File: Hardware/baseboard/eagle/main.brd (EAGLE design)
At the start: 119.5 x 96 mm, 169 parts, among them X1 JST-4POS-2X4POS, X1.2 TACH/LAP, X2 ATLAS-LTC, X2.1 MOTOR, X2.2 VRAILS+, X2.3 5V+SoC, X3 SYS-IIC, X4 SYSTEWI

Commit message: baseboard wip +did layout for 5V DCDC, was really fun to do, TI know their sh…tuff +now integrating into baseboard
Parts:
- added D1: BAS40-05, diode:SOT23
- moved A9:R2 420.6 mm to (79.5, 70.5), turned to 90 degrees
- moved A9:C5 416.9 mm to (77.9, 70.3), turned to 270 degrees
- moved A9:C4 24.6 mm to (89.9, 70.0)
- moved A9:C1 22.9 mm to (74.6, 71.8), turned to 270 degrees
- moved A9:C3 22.0 mm to (87.8, 70.0)
- moved A9:C2 19.5 mm to (85.7, 70.0)
- moved A9:U1 16.9 mm to (82.5, 69.8), turned to 270 degrees
- moved A9:R1 6.94 mm to (82.7, 67.0)
- moved A9:L1 0.56 mm to (79.7, 76.4)
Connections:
- net A9:N$1 renamed A9:CC
- removed net TOP.V+/IPC: A5:R8.2, A5:T2.5, A5:T2.6, A5:T2.7, A5:T2.8, A5:U1.17, S1.2
- new net +4.1V: A5:R8.2, A5:T2.5, A5:T2.6, A5:T2.7, A5:T2.8, A5:U1.17, D1.2, S1.2
- new net N$1: D1.3, X4.1
- net VDD: now also D1.1; no longer X4.1
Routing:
- net +4.1V: track 0.00 -> 42.2 mm, vias 0 -> 2
- net +5V: track 0.00 -> 11.4 mm
- net GND: track 10.0 -> 18.3 mm, vias 6 -> 32
- net A9:✳SW: track 0.00 -> 6.52 mm
- net TOP.V+/IPC: track 4.19 -> 0.00 mm
- net A9:CC: track 0.00 -> 4.09 mm
- net N$1: track 0.00 -> 2.50 mm
- net TOP.INACT: track 0.00 -> 2.17 mm
- added copper zone on layer 1, net +5V
- added copper zone on layer 1, net A9:CC
- added copper zone on layer 1, net A9:✳SW
- added copper zone on layer 1, net VDD
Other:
- board text added: "-> TI's got it down, look up their ref design: think altpart compatible landing pattern"
- board text added: ">thermal via tree algorithm?"
- board text added: "TODO ADD OPT. FB NETWORK BECAUSE LAYOUT"
- board text added: "TODO for final phase: Add stopmask extension for all inductors"
- board text added: "to minimize via/area cost?"
- board text removed: "embedded"
- board text removed: "interface"
- board text removed: "system"
- board text removed: "this was a typo initially"
- board text removed: "two-wire"
- board text removed: "wake-able IRQ"

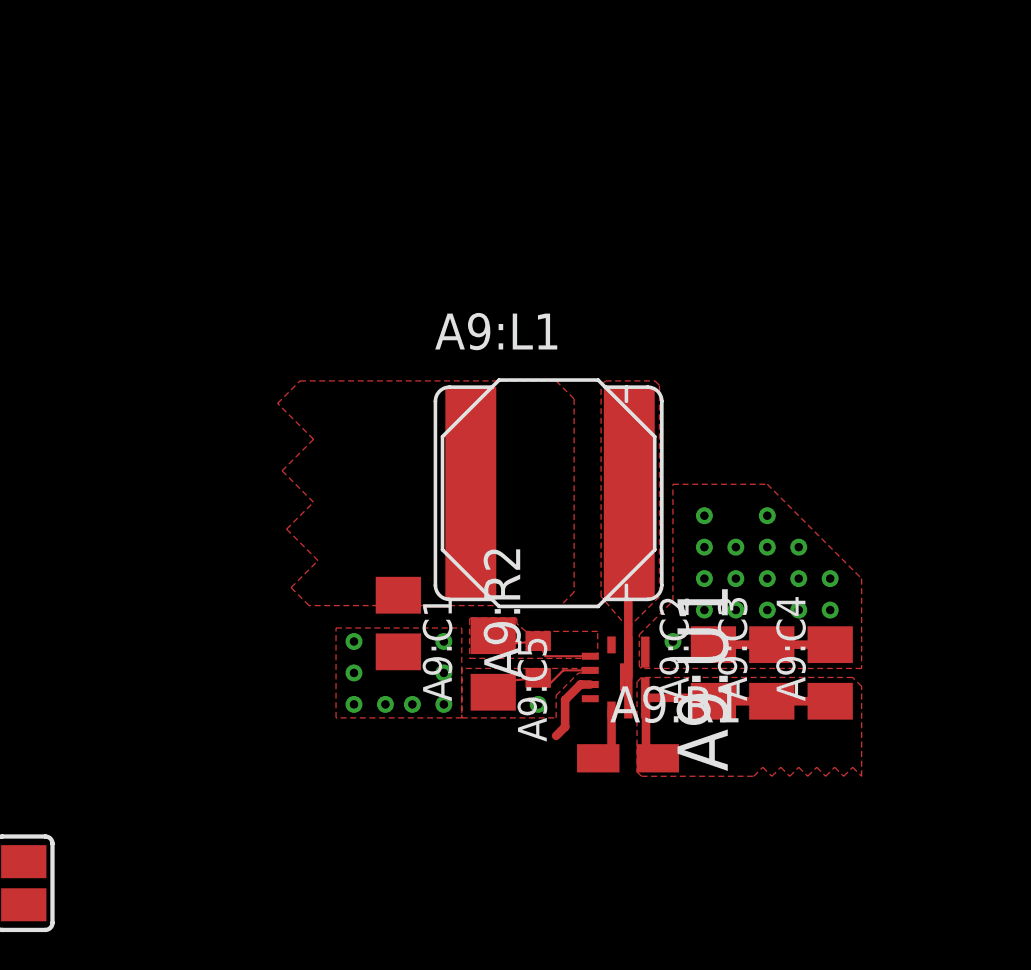
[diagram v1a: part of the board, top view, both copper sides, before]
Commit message: wip of baseboard + had to flip inductor on 5vdcdc because screw post is in the way + more chance it'll fit now
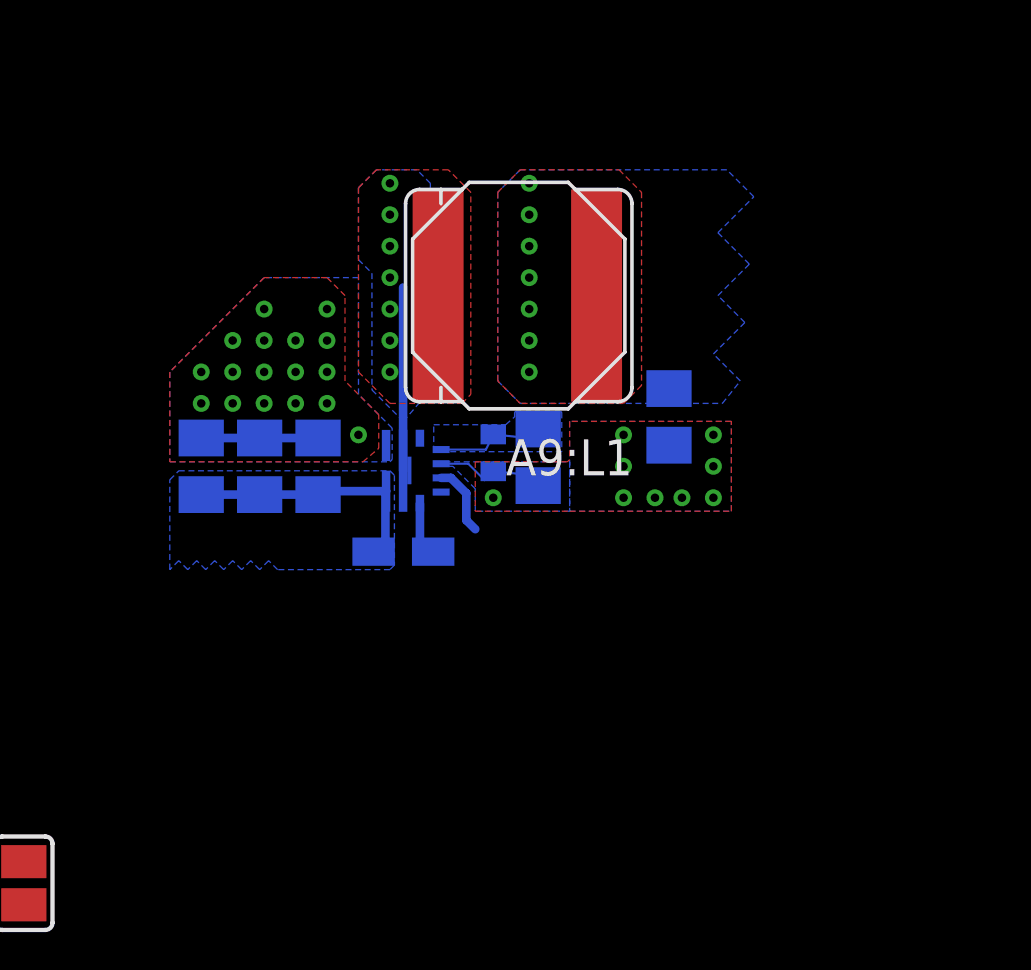
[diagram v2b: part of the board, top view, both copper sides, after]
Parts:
- moved A9:C4 23.4 mm to (67.6, 77.3), flipped to the bottom
- moved A9:C3 19.5 mm to (69.7, 77.3), flipped to the bottom
- moved A9:C2 15.8 mm to (71.8, 77.3), flipped to the bottom
- moved A9:C1 12.0 mm to (84.2, 79.1), flipped to the bottom
- moved A9:R1 10.8 mm to (74.8, 74.3), flipped to the bottom
- moved A9:U1 10.6 mm to (74.9, 77.2), flipped to the bottom
- moved A9:C5 7.47 mm to (79.5, 77.6), flipped to the bottom
- moved A9:R2 7.47 mm to (77.9, 77.8), flipped to the bottom
- moved A9:L1 7.01 mm to (79.1, 83.3), turned to 180 degrees
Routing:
- net A9:✳SW: track 6.52 -> 6.48 mm, vias 0 -> 7
- net VDD: vias 2 -> 9
- added copper zone on layer 16, net +5V
- added copper zone on layer 16, net A9:CC
- added copper zone on layer 16, net A9:✳SW
- added copper zone on layer 16, net VDD
- removed copper zone on layer 1, net +5V
- removed copper zone on layer 1, net A9:CC
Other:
- board text added: "going to flip my shit (ノ°Д°）ノ︵ ┻━┻"
- board text removed: ">thermal via tree algorithm?"
- board text removed: "to minimize via/area cost?"

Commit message: wip baseboard/quicksave + touchdown of dcdc   (quicksave means restore point)
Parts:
- moved A9:C1 89.0 mm to (18.8, 18.6), turned to 90 degrees
- moved A9:L1 88.4 mm to (23.9, 14.3), turned to 0 degrees
- moved A9:C5 80.4 mm to (23.4, 20.0), turned to 90 degrees
- moved A9:R2 78.5 mm to (25.0, 19.9), turned to 270 degrees
- moved A9:U1 73.5 mm to (28.0, 20.5), turned to 90 degrees
- moved A9:C2 69.9 mm to (31.2, 20.3), turned to 270 degrees
- moved A9:R1 69.4 mm to (28.2, 22.8), turned to 180 degrees
- moved A9:C3 67.6 mm to (33.3, 20.3), turned to 270 degrees
- moved A9:C4 65.5 mm to (35.3, 20.3), turned to 270 degrees
- moved REF1 1.12 mm to (-0.06, 0.08)
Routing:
- net TOP.INACT: track 2.17 -> 1.67 mm
- net GND: vias 32 -> 33
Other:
- outline, holes or cut-outs redrawn
- board text added: "+5V"
- board text added: "182 airwires? i don't give a rats' nest."
- board text added: "SMALLER PACKAGE NOW!"
- board text added: "conf"

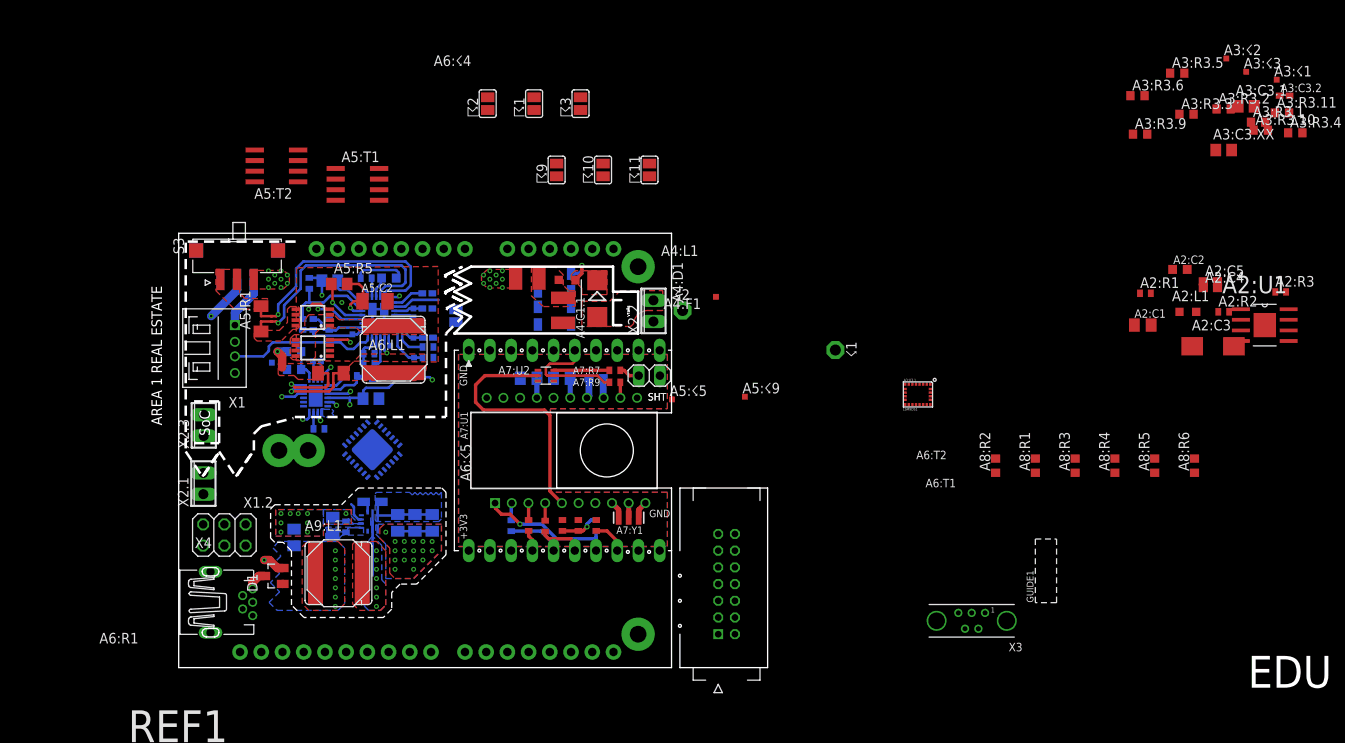
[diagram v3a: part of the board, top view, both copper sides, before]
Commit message: wip baseboard + as announced, added breakaway LTC connector + threw in molex/wirepad power thing too   because it looks symmetrical and the fab house would like   the board to be rectangular I guess
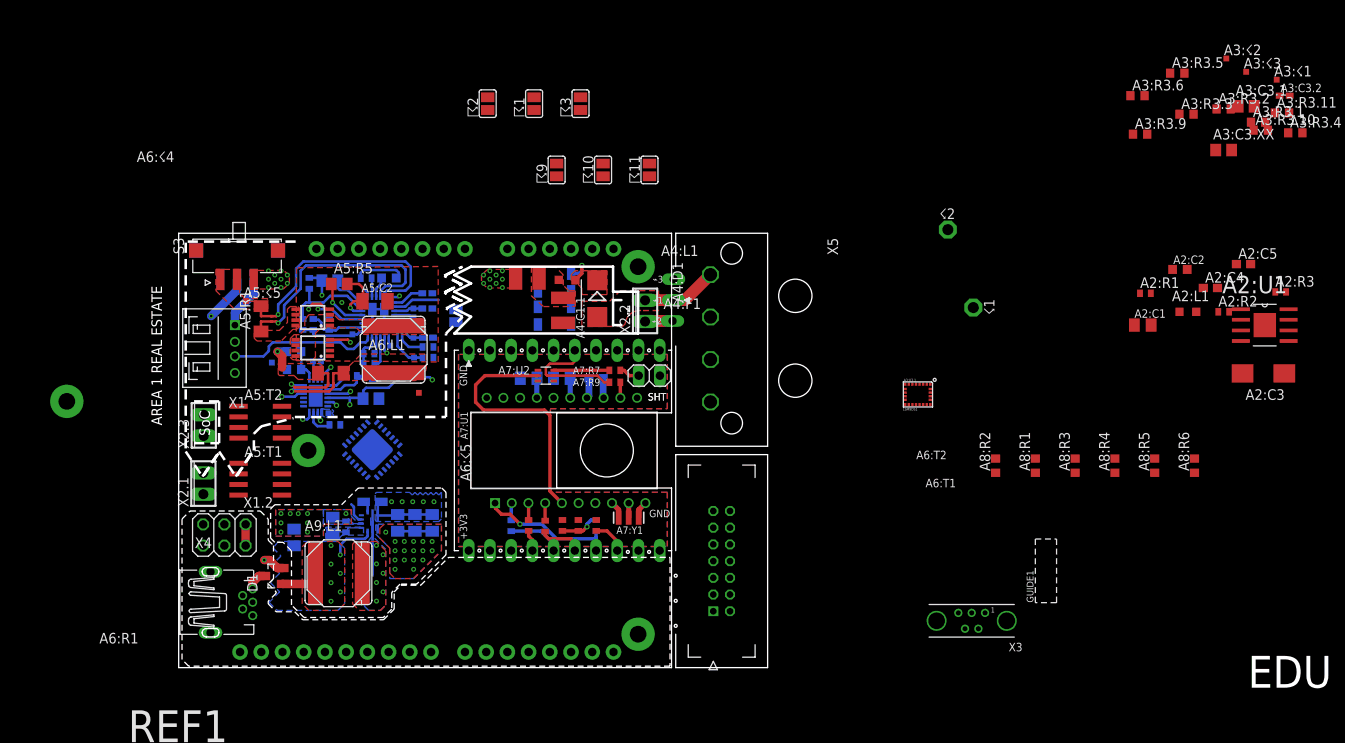
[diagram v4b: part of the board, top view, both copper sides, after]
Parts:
- added X5: 15244441, kitt.con:MOLEX_15244441
- added ⌁1: SINGLEPAD40MIL-BREAK.PILOT, kitt.con:PAD40MIL.BREAK_PILOT
- added ⌁2, ⌁3: SINGLEPAD40MIL-BREAK, kitt.con:PAD40MIL.BREAK
- moved A5:☇5 52.3 mm to (13.1, 46.9)
- moved A5:☇9 49.9 mm to (22.9, 33.4), flipped to the bottom
- moved A6:☇4 37.4 mm to (33.8, 35.9)
- moved A5:T1 37.2 mm to (14.8, 25.6)
- moved ☇2 33.2 mm to (97.1, 55.4)
- moved A5:T2 30.7 mm to (14.8, 32.4), turned to 270 degrees
- moved ☇1 17.3 mm to (100.1, 46.1)
- moved A2:C3 6.85 mm to (134.9, 38.2), turned to 180 degrees
- moved A2:C5 4.47 mm to (132.5, 51.3)
- moved X2 2.81 mm to (70.0, 15.8)
- moved A6:C1 1.96 mm to (23.7, 32.1)
- moved X2.2 1.00 mm to (60.8, 45.7)
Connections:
- net +5V: now also X5.4, ⌁3.P$1
- net GND: now also X5.2, X5.3, ⌁2.P$1
- net VCC/2: now also X5.1, ⌁1.P$1
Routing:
- net VCC/2: track 0.00 -> 9.10 mm
- net VDD: track 15.3 -> 23.9 mm
- net GND: track 18.3 -> 26.3 mm
- net +3V3: track 11.3 -> 13.9 mm
- net VF+OUT/SWITCH: track 0.00 -> 2.03 mm
- net +5V: track 11.2 -> 13.0 mm
- net A6:TRACK/SS: track 2.00 -> 3.38 mm
- added copper zone on layer 15, net +5V
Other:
- outline, holes or cut-outs redrawn
- board text added: "A BUNCH OF WIRES"
- board text added: "AREA 4: LOGIC"
- board text added: "…this isn't working. ~ Gabe N."
- board text removed: "SMALLER PACKAGE NOW!"

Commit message: wip baseboard quicksave  + now working on motor driver  + board area left is really, really tiny  + totally doable tough
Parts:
- removed X3: SYS-IIC, kitt.con:651005136421
- moved A5:T2 57.8 mm to (23.7, 89.5)
- moved A5:T1 56.6 mm to (23.7, 81.4)
- moved A2:C5 20.5 mm to (115.4, 40.0), flipped to the bottom, turned to 270 degrees
- moved A2:C3 17.6 mm to (119.2, 46.2), flipped to the bottom
- moved A2:U1 15.1 mm to (120.1, 41.4), turned to 180 degrees
- moved A2:R3 14.8 mm to (124.1, 40.7), flipped to the bottom, turned to 270 degrees
- moved A2:C4 14.1 mm to (115.4, 43.3), flipped to the bottom, turned to 270 degrees
- moved A2:C2 11.8 mm to (113.1, 50.2), flipped to the bottom
- moved A2:C1 10.8 mm to (113.0, 51.9), flipped to the bottom
- moved A2:L1 9.87 mm to (116.6, 49.2), flipped to the bottom, turned to 180 degrees
- moved A2:R2 8.98 mm to (122.6, 40.7), flipped to the bottom, turned to 270 degrees
- moved A2:R1 4.39 mm to (122.6, 43.8), flipped to the bottom, turned to 90 degrees
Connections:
- net N$2 renamed TOP.MOT-
- net N$4 renamed TOP.MOT+
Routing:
- net GND: track 26.3 -> 27.3 mm
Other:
- board size 119.5 x 96 mm -> 169.7 x 96 mm
- board text added: "+"
- board text added: "+18V fiy"
- board text added: "-"
- board text added: "AREA 6: MOTOR DRIVER"
- board text added: "CTRL"
- board text added: "Important design note: Power components must be on top layer: -> airflow and passive cooling"
- board text added: "VRAIL"
- board text added: "mot"
- board text added: "motdriver proto area"
- board text added: "soc"
- board text added: "well, another shunt track damn"
- board text removed: "going to flip my shit (ノ°Д°）ノ︵ ┻━┻"
- board text removed: "…this isn't working. ~ Gabe N."

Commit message: wip baseboard qucksave  + placement for motor driver good enough  + touchdown now into baseboard  + everything's fine
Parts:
- moved SJ1 52.7 mm to (120.5, 44.5), turned to 270 degrees
- moved A2:C1 14.2 mm to (127.0, 49.4), flipped to the top, turned to 270 degrees
- moved A2:C2 8.90 mm to (122.0, 50.7), flipped to the top
- moved A2:U1 6.46 mm to (125.9, 44.4)
- moved A2:R3 5.86 mm to (129.0, 43.9)
- moved A2:C3 5.86 mm to (124.1, 49.3)
- moved A2:C4 5.86 mm to (120.3, 46.5)
- moved A2:C5 5.86 mm to (120.3, 43.2)
- moved A2:R1 5.86 mm to (127.5, 47.0)
- moved A2:R2 5.86 mm to (127.5, 43.8)
- moved A2:L1 5.49 mm to (122.1, 49.2), flipped to the top, turned to 0 degrees
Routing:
- net GND: track 27.3 -> 26.3 mm
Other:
- board size 169.7 x 96 mm -> 174.7 x 97.2 mm

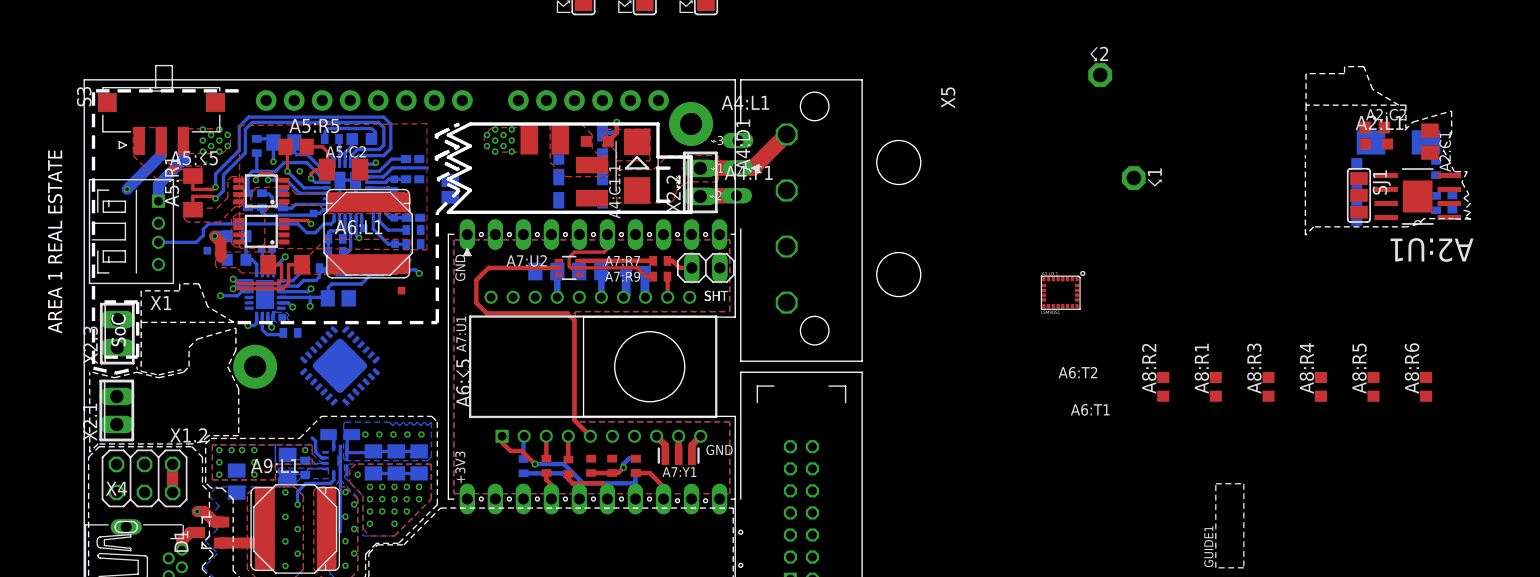
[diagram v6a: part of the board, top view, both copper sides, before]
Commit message: wip baseboard  + rough integration of motor driver done  + routes make sense, in a really, really unanticipated way    (for example, the thermal ground)
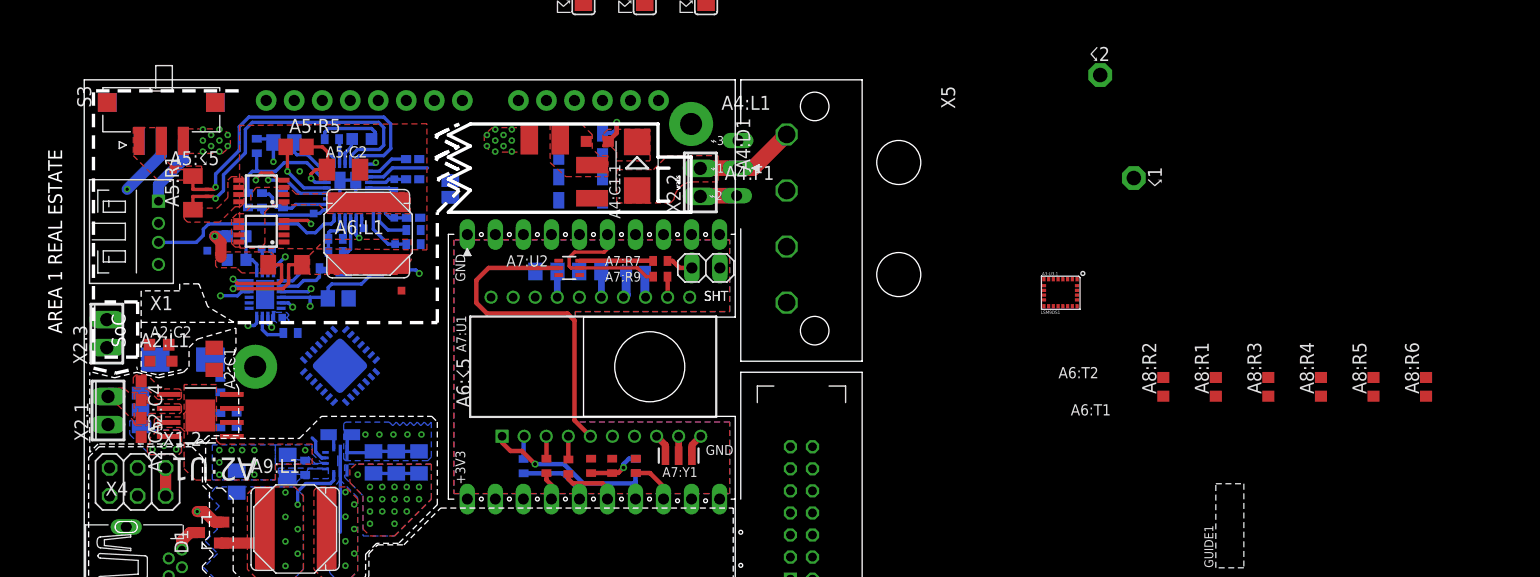
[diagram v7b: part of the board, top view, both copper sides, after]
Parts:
- moved SJ1 112.1 mm to (10.1, 25.1), flipped to the bottom
- moved A2:U1 112.1 mm to (15.5, 24.6)
- moved A2:C1 111.9 mm to (16.8, 29.7)
- moved A2:R3 111.9 mm to (18.8, 24.2)
- moved A2:C2 111.9 mm to (11.8, 31.0)
- moved A2:C3 111.9 mm to (13.9, 29.6)
- moved A2:C4 111.9 mm to (10.2, 26.8), flipped to the top
- moved A2:C5 111.9 mm to (10.2, 23.5), flipped to the top
- moved A2:L1 111.9 mm to (12.0, 29.5)
- moved A2:R1 111.9 mm to (17.3, 27.3)
- moved A2:R2 111.9 mm to (17.3, 24.2)
- moved X2.3 0.95 mm to (7.05, 32.0)
- moved X2.1 0.79 mm to (7.16, 25.0)
- moved X1.2 0.71 mm to (9.84, 18.6)
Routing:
- added copper zone on layer 1, net A2:VM
- added copper zone on layer 1, net TOP.MOT+
- added copper zone on layer 1, net TOP.MOT-
- added copper zone on layer 16, net TOP.MOT-
- added copper zone on layer 2, net TOP.MOT-
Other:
- board size 174.7 x 97.2 mm -> 119.5 x 96 mm
- board text removed: "+"
- board text removed: "-"
- board text removed: "CTRL"
- board text removed: "mot"
- board text removed: "motdriver proto area"
- board text removed: "soc"
